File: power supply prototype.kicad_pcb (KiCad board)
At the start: 4 copper layers, 72 x 50 mm, 28 parts, among them J1 Banana Plug, U1 MAX200008A

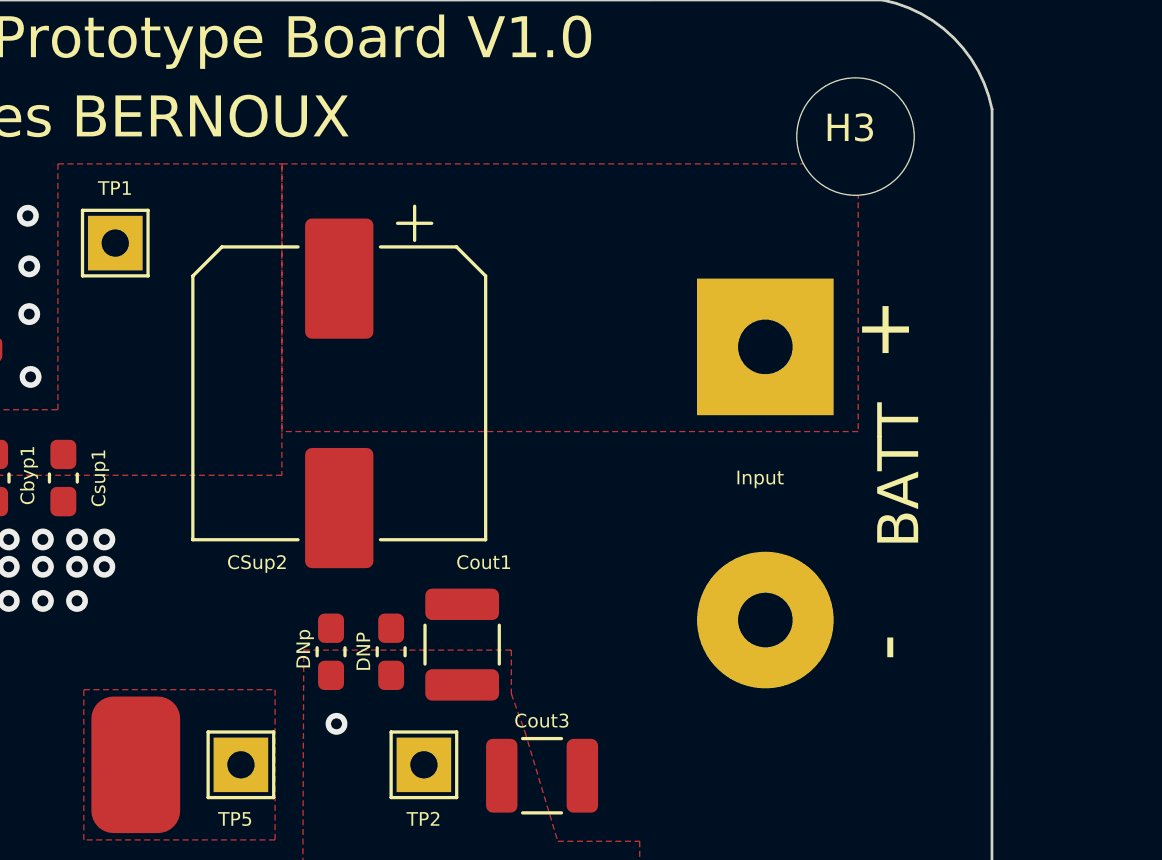
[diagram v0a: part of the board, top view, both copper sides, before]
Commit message: MAX20008 dev board update
Added reverse polarity protection diode on the input.
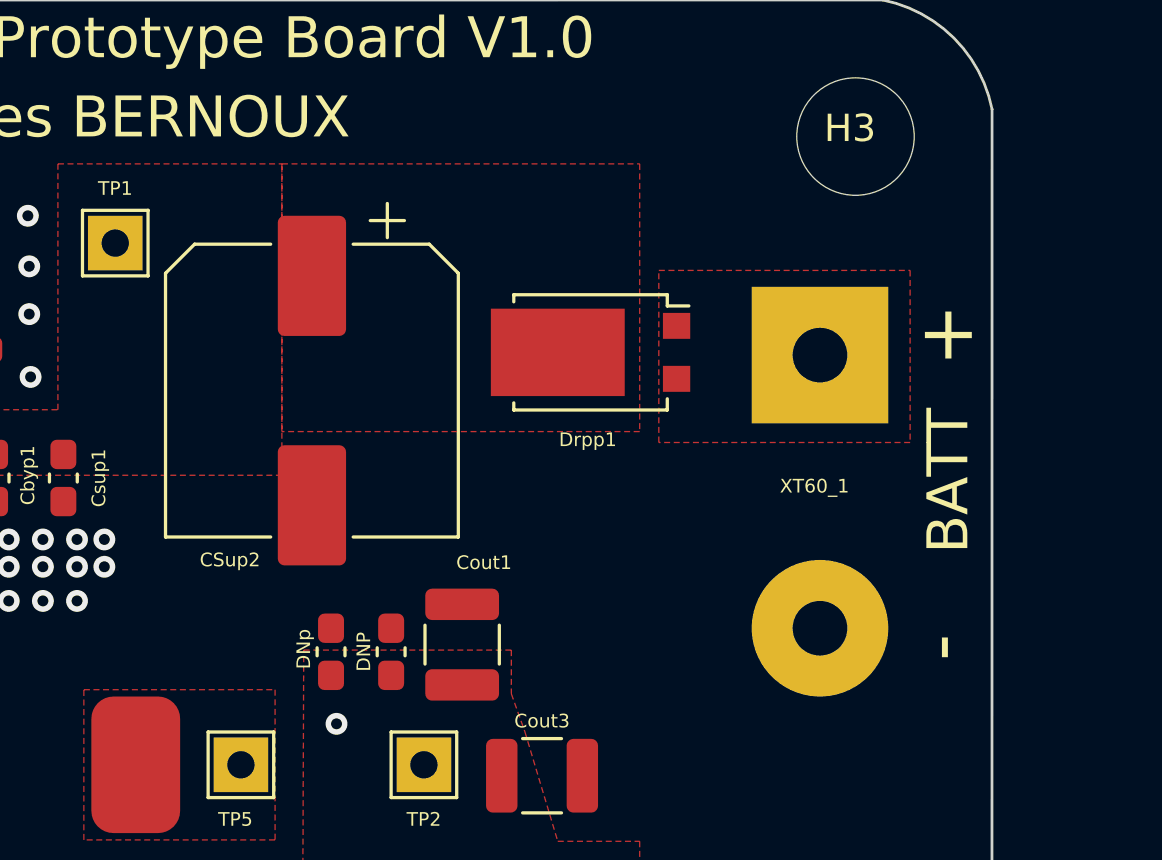
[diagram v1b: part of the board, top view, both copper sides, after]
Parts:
- added Drpp1: SB1060L, footprints:TO_277B, F.Cu at (157.3, 80.9)
- moved XT60_1 2.02 mm to (165.7, 86.0)
- moved CSup2 1.00 mm to (147.1, 82.3)
- renumbered Input to XT60_1
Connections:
- XT60_1 pad 1: +BATT -> Net-(Drpp1-Pad2)
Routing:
- added copper zone on F.Cu, net Net-(Drpp1-Pad2)
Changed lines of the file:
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@@
     (pad_to_mask_clearance 0)
     (pcbplotparams
-      (layerselection 0x00010fc_ffffffff)
+      (layerselection 0x00010a8_ffffffff)
       (disableapertmacros false)
       (usegerberextensions false)
@@
       (drillshape 0)
       (scaleselection 1)
-      (outputdirectory "output files/pos files/")
+      (outputdirectory "Gerbers/")
     )
   )
@@
   (net 10 "/power supply/RESET")
   (net 11 "Net-(L1-Pad2)")
+  (net 12 "Net-(Drpp1-Pad2)")
   (footprint "LOGO" (layer "F.Cu")
     (at 111.333978 91.24076)
     (attr board_only exclude_from_pos_files exclude_from_bom)
     (fp_text reference "G***" (at -1.3 12.2) (layer "User.1") hide
-      (effects (font (size 1.524 1.524)))
+      (effects (font (size 1.524 1.524) (thickness 0.15)))
     )
     (fp_text value "LOGO" (at 0.75 0) (layer "F.SilkS") hide
@@
   )
   (footprint "Capacitor_SMD:CP_Elec_10x10.5" (layer "F.Cu")
-    (at 148.1 82.4 -90)
+    (at 147.1 82.3 -90)
     (descr "SMD capacitor, aluminum electrolytic, Vishay 1010, 10.0x10.5mm, http://www.vishay.com/docs/28395/150crz.pdf")
     (tags "capacitor electrolytic")
@@
     )
   )
+  (footprint "footprints:TO_277B" (layer "F.Cu")
+    (at 157.3 80.9 -90)
+    (descr "TO-227B https://media.digikey.com/pdf/Data%20Sheets/Littelfuse%20PDFs/DST2050S.pdf")
+    (tags "TO-277B")
+    (property "Sheetfile" "File: power_supply.kicad_sch")
+    (property "Sheetname" "power supply")
+    (attr smd)
+    (fp_text reference "Drpp1" (at 3.2 0.1 180) (layer "F.SilkS")
+      (effects (font (size 0.5 0.5) (thickness 0.1)))
+    )
+    (fp_text value "SB1060L" (at 0 4.7 90) (layer "F.Fab")
+      (effects (font (size 1 1) (thickness 0.15)))
+    )
+    (fp_text user "${REFERENCE}" (at 0 0 90) (layer "F.Fab")
+      (effects (font (size 0.9 0.9) (thickness 0.15)))
+    )
+    (fp_line (start 2.11 -2.81) (end 1.7 -2.81) (layer "F.SilkS") (width 0.12))
+    (fp_line (start -1.85 2.81) (end -2.11 2.81) (layer "F.SilkS") (width 0.12))
+    (fp_line (start -2.11 -2.81) (end -2.11 2.81) (layer "F.SilkS") (width 0.12))
+    (fp_line (start -1.7 -2.81) (end -2.11 -2.81) (layer "F.SilkS") (width 0.12))
+    (fp_line (start 2.11 2.81) (end 1.85 2.81) (layer "F.SilkS") (width 0.12))
+    (fp_line (start -1.7 -2.81) (end -1.7 -3.6) (layer "F.SilkS") (width 0.12))
+    (fp_line (start 2.11 2.81) (end 2.11 -2.81) (layer "F.SilkS") (width 0.12))
+    (fp_line (start -2.24 -2.94) (end -1.7 -2.94) (layer "F.CrtYd") (width 0.05))
+    (fp_line (start -2.24 2.94) (end -1.85 2.94) (layer "F.CrtYd") (width 0.05))
+    (fp_line (start 2.24 2.94) (end 2.24 -2.94) (layer "F.CrtYd") (width 0.05))
+    (fp_line (start 1.85 2.94) (end 2.24 2.94) (layer "F.CrtYd") (width 0.05))
+    (fp_line (start 1.85 3.9) (end -1.85 3.9) (layer "F.CrtYd") (width 0.05))
+    (fp_line (start 1.7 -2.94) (end 2.24 -2.94) (layer "F.CrtYd") (width 0.05))
+    (fp_line (start -1.85 3.9) (end -1.85 2.94) (layer "F.CrtYd") (width 0.05))
+    (fp_line (start -2.24 -2.94) (end -2.24 2.94) (layer "F.CrtYd") (width 0.05))
+    (fp_line (start 1.7 -2.94) (end 1.7 -3.9) (layer "F.CrtYd") (width 0.05))
+    (fp_line (start -1.7 -2.94) (end -1.7 -3.9) (layer "F.CrtYd") (width 0.05))
+    (fp_line (start 1.85 3.9) (end 1.85 2.94) (layer "F.CrtYd") (width 0.05))
+    (fp_line (start -1.7 -3.9) (end 1.7 -3.9) (layer "F.CrtYd") (width 0.05))
+    (fp_line (start -1.99 2.69) (end 1.99 2.69) (layer "F.Fab") (width 0.1))
+    (fp_line (start 1.99 2.69) (end 1.99 -2.69) (layer "F.Fab") (width 0.1))
+    (fp_line (start -1.99 -1.69) (end -1.99 2.69) (layer "F.Fab") (width 0.1))
+    (fp_line (start -1.99 -1.69) (end -0.99 -2.69) (layer "F.Fab") (width 0.1))
+    (fp_line (start 1.99 -2.69) (end -1 -2.69) (layer "F.Fab") (width 0.1))
+    (pad "" smd rect (at -0.9 3 270) (size 1.3 1.2) (layers "F.Paste"))
+    (pad "" smd rect (at 0.9 1.2 270) (size 1.3 1.2) (layers "F.Paste"))
+    (pad "" smd rect (at 0.9 3 270) (size 1.3 1.2) (layers "F.Paste"))
+    (pad "" smd rect (at -0.9 -0.6 270) (size 1.3 1.2) (layers "F.Paste"))
+    (pad "" smd rect (at -0.9 1.2 270) (size 1.3 1.2) (layers "F.Paste"))
+    (pad "" smd rect (at 0.9 -0.6 270) (size 1.3 1.2) (layers "F.Paste"))
+    (pad "1" smd rect (at 0 1.2 270) (size 3.2 4.9) (layers "F.Cu" "F.Mask")
+      (net 5 "+BATT") (pinfunction "K") (pintype "passive"))
+    (pad "2" smd rect (at -0.97 -3.15 270) (size 0.95 1) (layers "F.Cu" "F.Paste" "F.Mask")
+      (net 12 "Net-(Drpp1-Pad2)") (pinfunction "A") (pintype "passive"))
+    (pad "2" smd rect (at 0.97 -3.15 270) (size 0.95 1) (layers "F.Cu" "F.Paste" "F.Mask")
+      (net 12 "Net-(Drpp1-Pad2)") (pinfunction "A") (pintype "passive"))
+    (model "${KICAD6_3DMODEL_DIR}/Package_TO_SOT_SMD.3dshapes/TO-277B.wrl"
+      (offset (xyz 0 0 0))
+      (scale (xyz 1 1 1))
+      (rotate (xyz 0 0 0))
+    )
+  )
   (footprint "TestPoint:TestPoint_THTPad_2.0x2.0mm_Drill1.0mm" (layer "F.Cu")
     (at 151.2 96)
@@
   )
   (footprint "footprints:XT60 conn" (layer "F.Cu")
-    (at 163.7 85.7 -90)
+    (at 165.7 86 -90)
     (property "Sheetfile" "File: power_supply.kicad_sch")
     (property "Sheetname" "power supply")
     (attr smd)
-    (fp_text reference "Input" (at -0.2 0.2 unlocked) (layer "F.SilkS")
+    (fp_text reference "XT60_1" (at -0.2 0.2 unlocked) (layer "F.SilkS")
       (effects (font (size 0.5 0.5) (thickness 0.1)))
     )
@@
     (fp_rect (start 8 -3) (end -8 3) (layer "F.Fab") (width 0.1) (fill none))
     (pad "1" thru_hole rect (at -5 0 270) (size 5 5) (drill 2) (layers *.Cu *.Mask)
-      (net 5 "+BATT") (pinfunction "Pin_1") (pintype "passive") (zone_connect 1))
+      (net 12 "Net-(Drpp1-Pad2)") (pinfunction "Pin_1") (pintype "passive") (zone_connect 1) (thermal_width 2))
     (pad "2" thru_hole oval (at 5 0 270) (size 5 5) (drill 2) (layers *.Cu *.Mask)
       (net 2 "-BATT") (pinfunction "Pin_2") (pintype "passive") (zone_connect 1) (thermal_width 1.3))
@@
   (gr_line (start 104.00555 117.994449) (end 167.994449 117.994449) (layer "Edge.Cuts") (width 0.1))
   (gr_arc (start 171.994449 113.99445) (mid 170.6 116.6) (end 167.994449 117.994449) (layer "Edge.Cuts") (width 0.1))
-  (gr_text "+" (at 168.1 80) (layer "F.SilkS")
+  (gr_text "+" (at 170.4 80.2) (layer "F.SilkS")
     (effects (font (size 2 2) (thickness 0.2)))
   )
@@
     (effects (font (size 1.5 1.5) (thickness 0.3)))
   )
-  (gr_text "-" (at 168.1 91.7 90) (layer "F.SilkS")
+  (gr_text "-" (at 170.1 91.7 90) (layer "F.SilkS")
     (effects (font (size 2 2) (thickness 0.2)))
   )
@@
     (effects (font (size 2 2) (thickness 0.2)))
   )
-  (gr_text "BATT \n" (at 168.6 85.4 90) (layer "F.SilkS")
+  (gr_text "BATT \n" (at 170.4 85.6 90) (layer "F.SilkS")
     (effects (font (size 1.5 1.5) (thickness 0.3)))
   )
@@
     )
   )
+  (zone (net 12) (net_name "Net-(Drpp1-Pad2)") (layer "F.Cu") (hatch edge 0.508)
+    (priority 2)
+    (connect_pads (clearance 0.2))
+    (min_thickness 0.254) (filled_areas_thickness no)
+    (fill yes (thermal_gap 0.2) (thermal_bridge_width 0.508))
+    (polygon
+      (pts
+        (xy 169 84.2)
+        (xy 159.8 84.2)
+        (xy 159.8 77.9)
+        (xy 169 77.9)
+      )
+    )
+  )
   (zone (net 5) (net_name "+BATT") (layer "F.Cu") (hatch edge 0.508)
     (priority 1)
@@
     (polygon
       (pts
-        (xy 167.1 83.8)
+        (xy 159.1 83.8)
         (xy 146 83.8)
         (xy 146 74)
-        (xy 167.1 74)
+        (xy 159.1 74)
       )
     )
